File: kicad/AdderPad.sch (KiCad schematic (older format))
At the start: 1 part

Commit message: Finished PCB
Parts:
- added D1, D2, D3, D4, D5, D6, D7, D8: D_Small, Keebio-Parts:Diode, symbol Device:D_Small
- added MX1, MX2, MX3, MX4, MX5, MX6, MX7, MX8: MX-NoLED, MX_Only:MXOnly-1U-Hotswap, symbol MX_Alps_Hybrid:MX-NoLED
- added SW1: SW_Push, Button_Switch_THT:KSA_Tactile_SPST, symbol Switch:SW_Push
- U1: renamed from U?; footprint (none) -> Keebio-Parts:ArduinoProMicro
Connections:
- net ROW1: now reaches U1.15 (14/PB3)
- net ROW1: now also D5.1 (K), D6.1 (K), D7.1 (K), D8.1 (K)
- net COL3: now reaches U1.16 (15/PB1)
- net COL3: now also MX4.1 (COL), MX8.1 (COL)
- net COL2: now reaches U1.17 (A0/PF7)
- net COL2: now also MX3.1 (COL), MX7.1 (COL)
- net COL1: now reaches U1.18 (A1/PF6)
- net COL1: now also MX2.1 (COL), MX6.1 (COL)
- net COL0: now reaches U1.19 (A2/PF5)
- net COL0: now also MX1.1 (COL), MX5.1 (COL)
- net ROW0: now reaches U1.20 (A3/PF4)
- net ROW0: now also D1.1 (K), D2.1 (K), D3.1 (K), D4.1 (K)
- net VCC: now reaches U1.21 (VCC)
- net reset: now reaches U1.22 (RST)
- net reset: now also SW1.1
- net GND: now reaches U1.23 (GND)
- net GND: now also U1.3 (GND), U1.4 (GND), SW1.2
- new net: D1.2 (A), MX1.2 (ROW)
- new net: D2.2 (A), MX2.2 (ROW)
- new net: D3.2 (A), MX3.2 (ROW)
- new net: D4.2 (A), MX4.2 (ROW)
- new net: D5.2 (A), MX5.2 (ROW)
- new net: D6.2 (A), MX6.2 (ROW)
- new net: D7.2 (A), MX7.2 (ROW)
- new net: D8.2 (A), MX8.2 (ROW)
- no-connect marks 0 -> 5

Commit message: Added angled reset button
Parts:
- SW1: footprint Button_Switch_THT:KSA_Tactile_SPST -> Keebio-Parts:SW_Tactile_SPST_Angled_MJTP1117
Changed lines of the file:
@@
 F 0 "SW1" H 5200 4235 50  0000 C CNN
 F 1 "SW_Push" H 5200 4144 50  0000 C CNN
-F 2 "Button_Switch_THT:KSA_Tactile_SPST" H 5200 4150 50  0001 C CNN
+F 2 "Keebio-Parts:SW_Tactile_SPST_Angled_MJTP1117" H 5200 4150 50  0001 C CNN
 F 3 "~" H 5200 4150 50  0001 C CNN
 	1    5200 3950

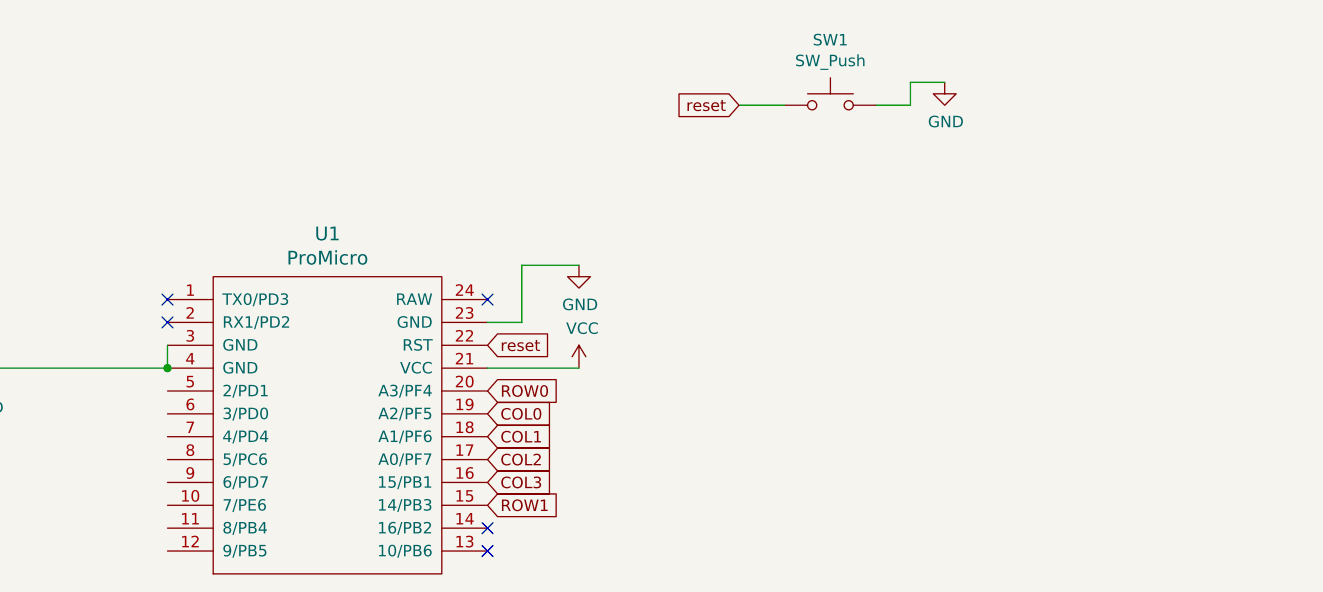
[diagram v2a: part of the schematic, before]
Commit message: Added RGB underglow LEDs
Rerouted traces, new mill sizes
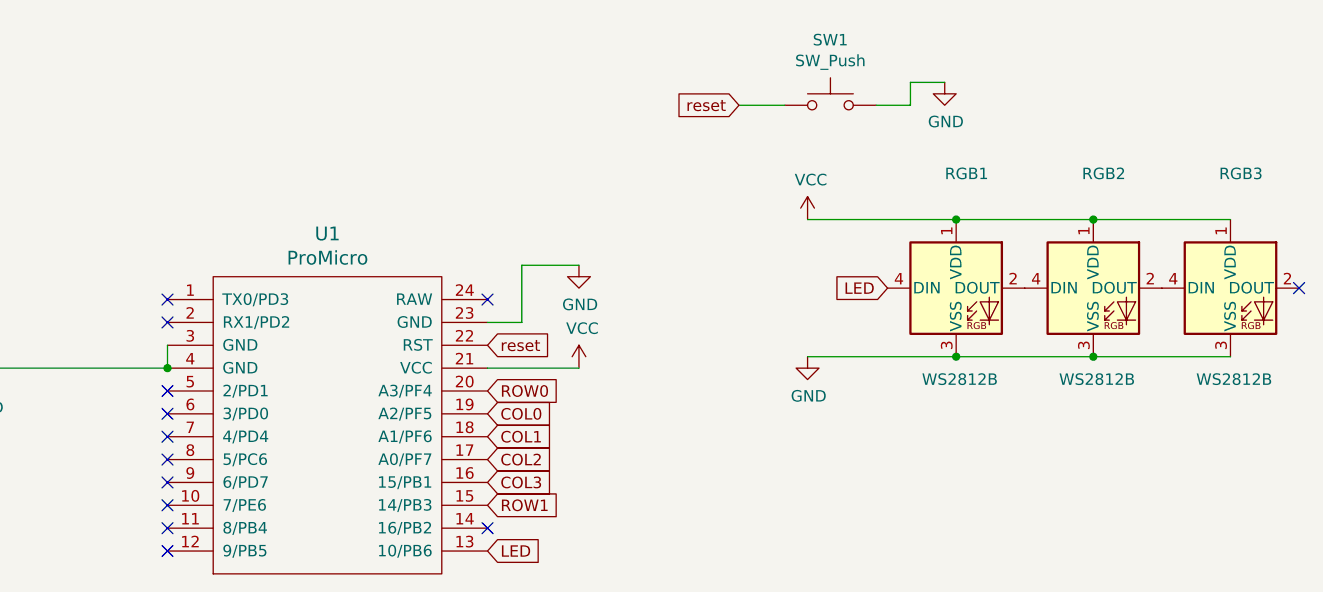
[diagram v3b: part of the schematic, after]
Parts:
- added RGB1, RGB2, RGB3: WS2812B, Keebio-Parts:WS2812B, symbol LED:WS2812B
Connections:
- net GND: now also RGB1.3 (VSS), RGB2.3 (VSS), RGB3.3 (VSS)
- net VCC: now also RGB1.1 (VDD), RGB2.1 (VDD), RGB3.1 (VDD)
- net LED: now reaches U1.13 (10/PB6)
- net LED: now also RGB1.4 (DIN)
- new net: RGB1.2 (DOUT), RGB2.4 (DIN)
- new net: RGB2.2 (DOUT), RGB3.4 (DIN)
- no-connect marks 5 -> 13
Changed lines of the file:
@@
 NoConn ~ 3700 4800
 NoConn ~ 2300 4900
-NoConn ~ 2300 4800
 $Comp
 L MX_Alps_Hybrid:MX-NoLED MX1
@@
 ROW0
 NoConn ~ 3700 5800
-NoConn ~ 3700 5900
 $Comp
 L Switch:SW_Push SW1
@@
 Text GLabel 3700 5000 2    50   Input ~ 0
 reset
+NoConn ~ 2300 5900
+NoConn ~ 2300 5800
+NoConn ~ 2300 5700
+NoConn ~ 2300 5600
+NoConn ~ 2300 5500
+NoConn ~ 2300 5400
+NoConn ~ 2300 5300
+NoConn ~ 2300 5200
+$Comp
+L LED:WS2812B RGB1
+U 1 1 61C1EB61
+P 5750 4750
+F 0 "RGB1" H 5700 5250 50  0000 L CNN
+F 1 "WS2812B" H 5600 4350 50  0000 L CNN
+F 2 "Keebio-Parts:WS2812B" H 5800 4450 50  0001 L TNN
+F 3 "https://cdn-shop.adafruit.com/datasheets/WS2812B.pdf" H 5850 4375 50  0001 L TNN
+	1    5750 4750
+	1    0    0    -1
+$EndComp
+$Comp
+L LED:WS2812B RGB2
+U 1 1 61C235F2
+P 6350 4750
+F 0 "RGB2" H 6300 5250 50  0000 L CNN
+F 1 "WS2812B" H 6200 4350 50  0000 L CNN
+F 2 "Keebio-Parts:WS2812B" H 6400 4450 50  0001 L TNN
+F 3 "https://cdn-shop.adafruit.com/datasheets/WS2812B.pdf" H 6450 4375 50  0001 L TNN
+	1    6350 4750
+	1    0    0    -1
+$EndComp
+$Comp
+L LED:WS2812B RGB3
+U 1 1 61C23CA7
+P 6950 4750
+F 0 "RGB3" H 6900 5250 50  0000 L CNN
+F 1 "WS2812B" H 6800 4350 50  0000 L CNN
+F 2 "Keebio-Parts:WS2812B" H 7000 4450 50  0001 L TNN
+F 3 "https://cdn-shop.adafruit.com/datasheets/WS2812B.pdf" H 7050 4375 50  0001 L TNN
+	1    6950 4750
+	1    0    0    -1
+$EndComp
+$Comp
+L power:GND #PWR0105
+U 1 1 61C24651
+P 5100 5050
+F 0 "#PWR0105" H 5100 4800 50  0001 C CNN
+F 1 "GND" H 5105 4877 50  0000 C CNN
+F 2 "" H 5100 5050 50  0001 C CNN
+F 3 "" H 5100 5050 50  0001 C CNN
+	1    5100 5050
+	1    0    0    -1
+$EndComp
+Wire Wire Line
+	5100 5050 5750 5050
+Connection ~ 5750 5050
+Wire Wire Line
+	5750 5050 6350 5050
+Connection ~ 6350 5050
+Wire Wire Line
+	6350 5050 6950 5050
+NoConn ~ 7250 4750
+$Comp
+L power:VCC #PWR0106
+U 1 1 61C271F9
+P 5100 4450
+F 0 "#PWR0106" H 5100 4300 50  0001 C CNN
+F 1 "VCC" H 5115 4623 50  0000 C CNN
+F 2 "" H 5100 4450 50  0001 C CNN
+F 3 "" H 5100 4450 50  0001 C CNN
+	1    5100 4450
+	1    0    0    -1
+$EndComp
+Wire Wire Line
+	5100 4450 5750 4450
+Connection ~ 5750 4450
+Wire Wire Line
+	5750 4450 6350 4450
+Connection ~ 6350 4450
+Wire Wire Line
+	6350 4450 6950 4450
+Text GLabel 5450 4750 0    50   Input ~ 0
+LED
+NoConn ~ 2300 4800
+Text GLabel 3700 5900 2    50   Input ~ 0
+LED
 $EndSCHEMATC

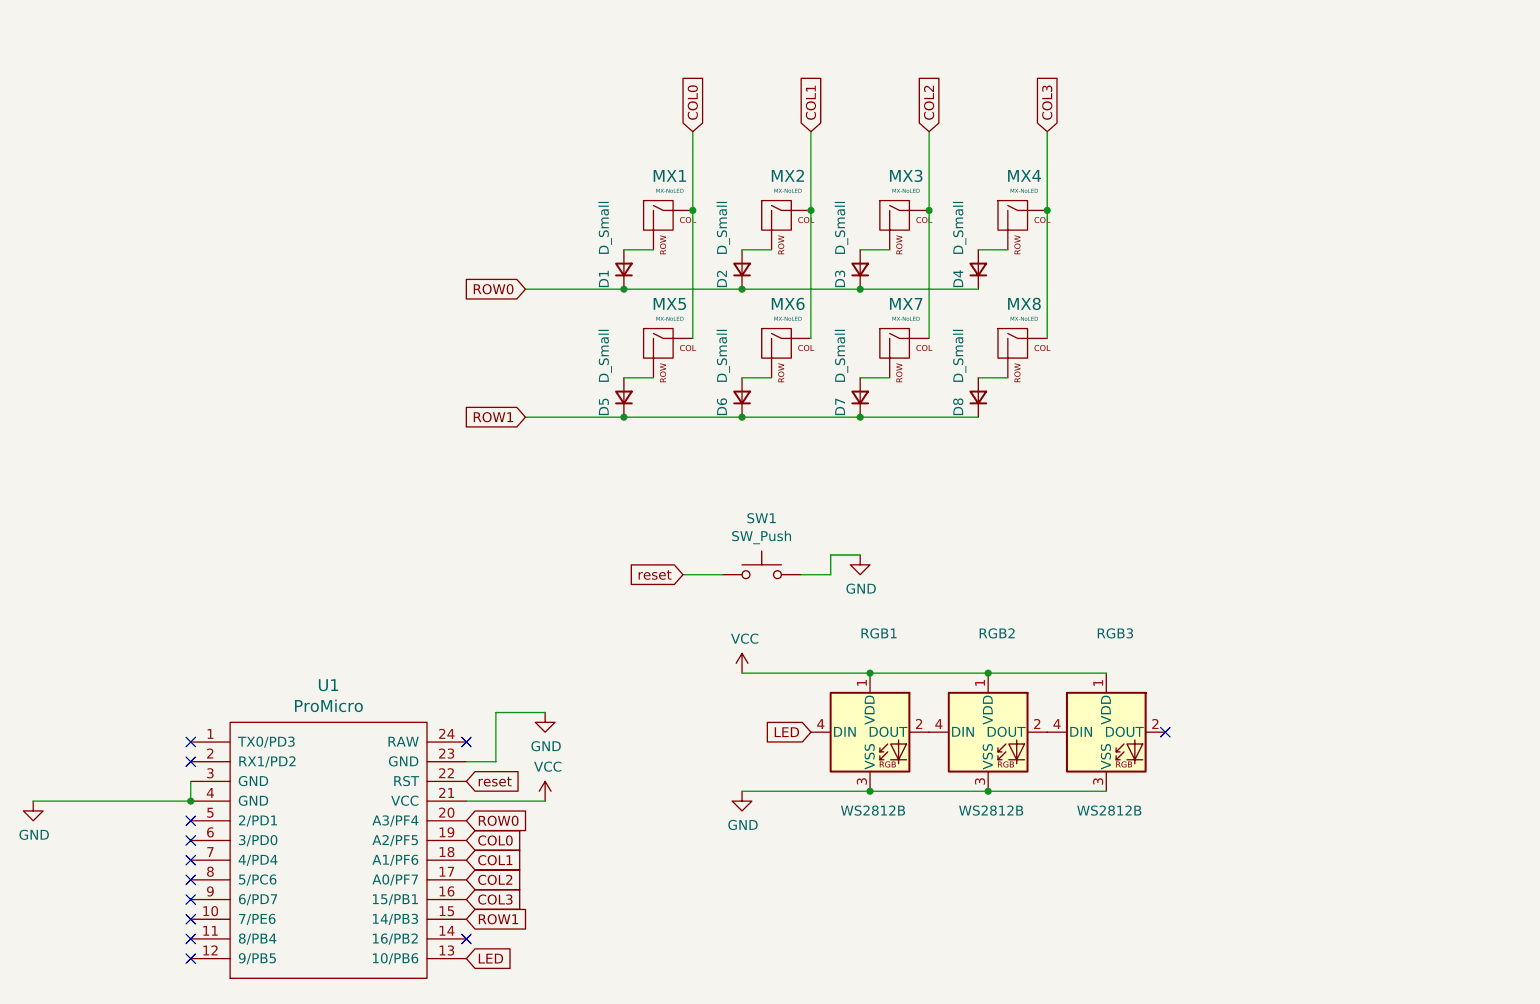
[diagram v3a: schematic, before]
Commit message: Multiple updates
- added 128x64 OLED support
- added fourth underglow RGB
- resize PCB
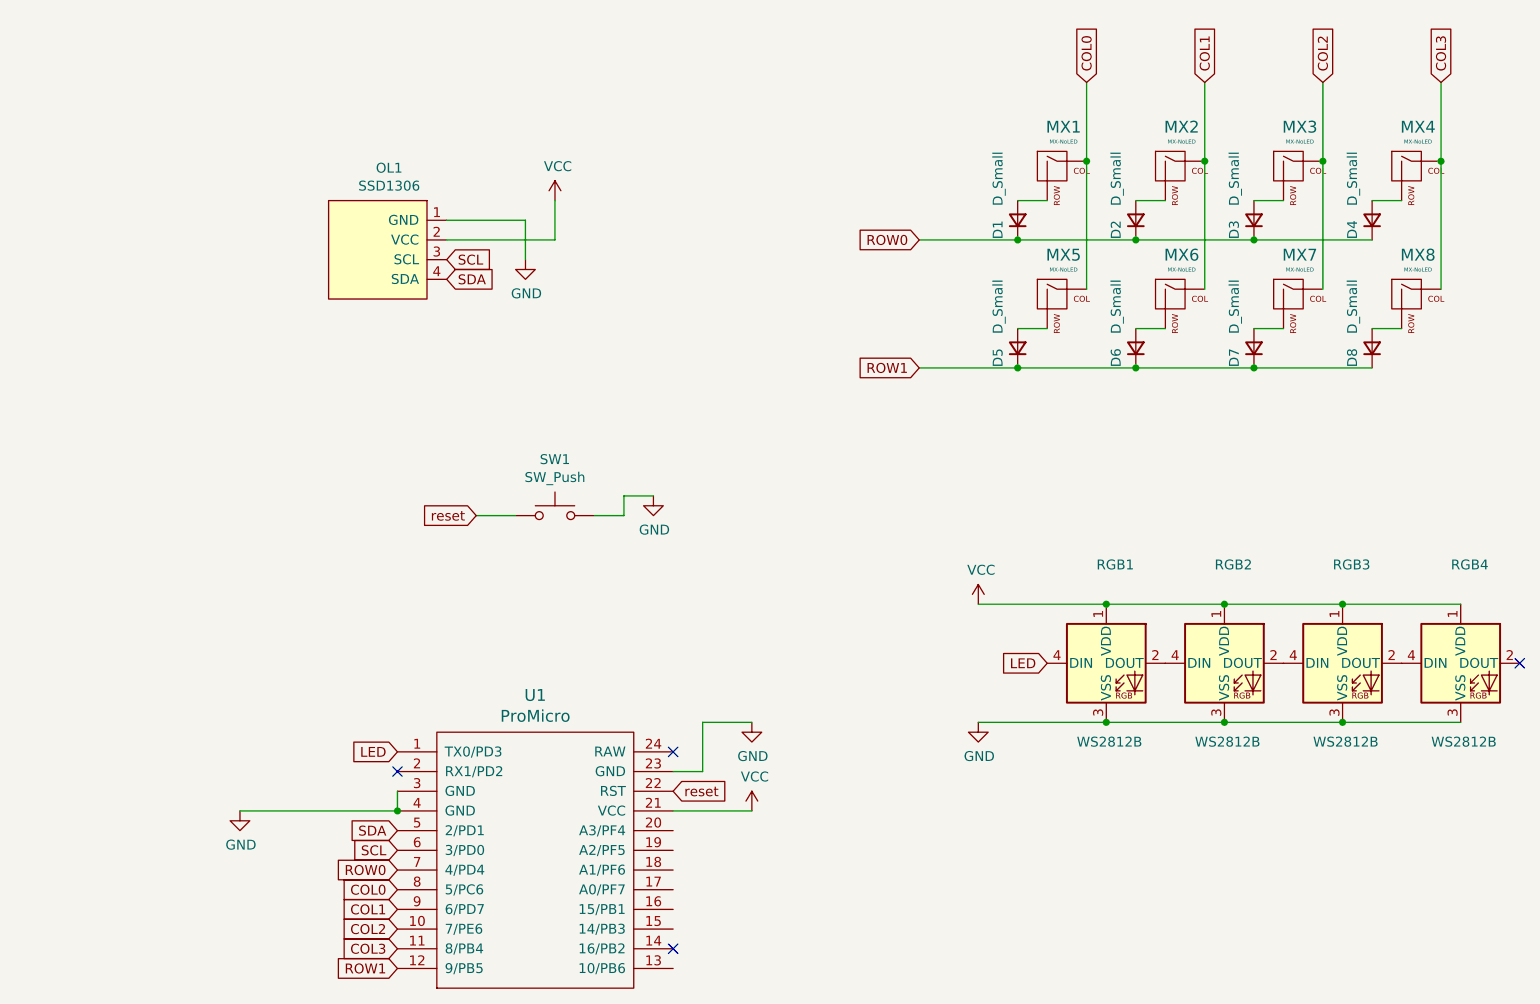
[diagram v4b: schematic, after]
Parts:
- added OL1: SSD1306, SSD1306:128x64OLED, symbol SSD1306-128x64_OLED:SSD1306
- added RGB4: WS2812B, Keebio-Parts:WS2812B, symbol LED:WS2812B
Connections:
- net COL0: now also U1.8 (5/PC6); no longer U1.19 (A2/PF5)
- net COL1: now also U1.9 (6/PD7); no longer U1.18 (A1/PF6)
- net COL2: now also U1.10 (7/PE6); no longer U1.17 (A0/PF7)
- net COL3: now also U1.11 (8/PB4); no longer U1.16 (15/PB1)
- net GND: now also OL1.1 (GND), RGB4.3 (VSS)
- net LED: now also U1.1 (TX0/PD3); no longer U1.13 (10/PB6)
- net ROW0: now also U1.7 (4/PD4); no longer U1.20 (A3/PF4)
- net ROW1: now also U1.12 (9/PB5); no longer U1.15 (14/PB3)
- net VCC: now also OL1.2 (VCC), RGB4.1 (VDD)
- net SDA: now reaches U1.5 (2/PD1)
- net SDA: now also OL1.4 (SDA)
- net SCL: now reaches U1.6 (3/PD0)
- net SCL: now also OL1.3 (SCL)
- net at RGB3.2 (DOUT): now also RGB4.4 (DIN)
- no-connect marks 13 -> 4
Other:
- moved on the sheet: D1, D2, D3, D4, D5, D6, D7, D8, MX1, MX2, MX3, MX4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
